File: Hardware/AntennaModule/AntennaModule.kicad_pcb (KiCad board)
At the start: 2 copper layers, 53 parts, among them J1 Conn_01x10, SW1 ColdStart, U1 C0727J5003AHF-1, U2 C0727J5003AHF-1, U3 NJG1155UX2, U4 NT1192FAAE1S, U5 PD0922J5050S2HF, U6 NT1192FAAE1S, U7 NEO-D9C, U8 NEO-F9P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

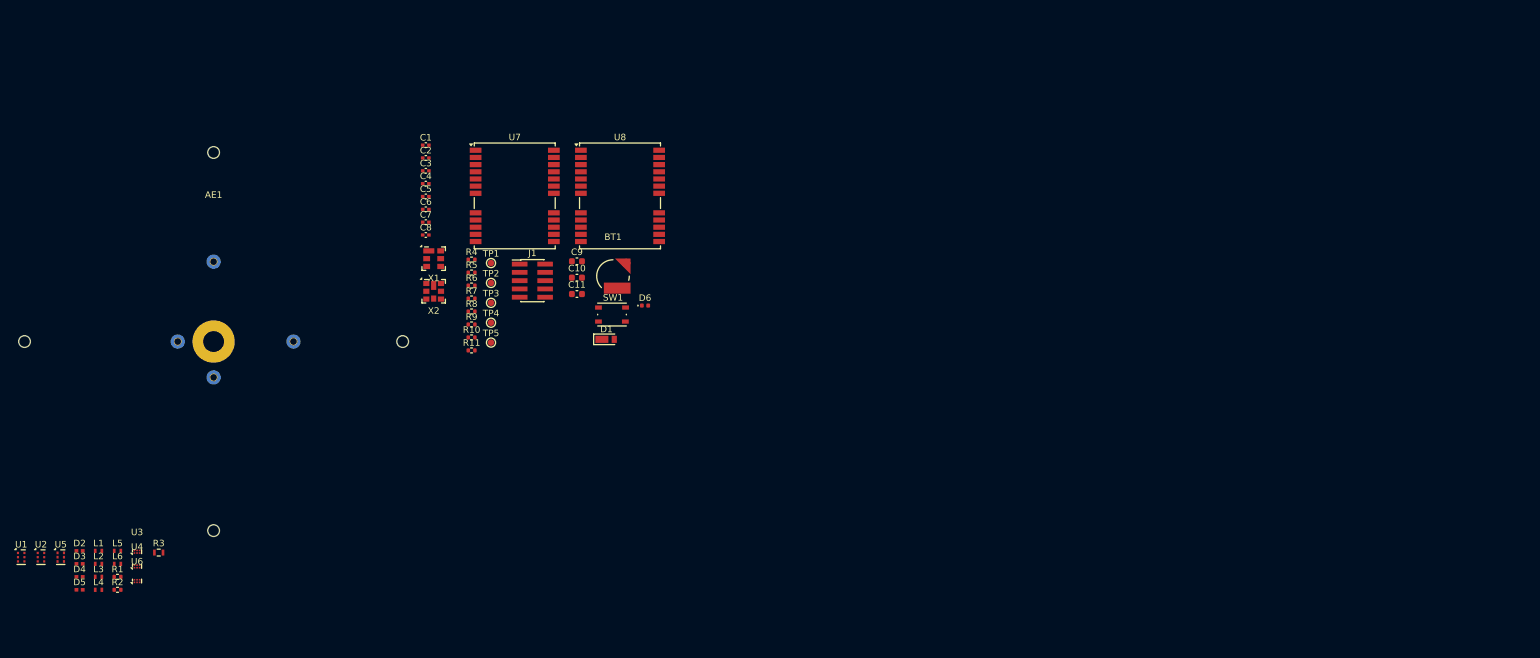
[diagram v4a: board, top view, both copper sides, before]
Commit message: グリッドとドリルの原点を設定
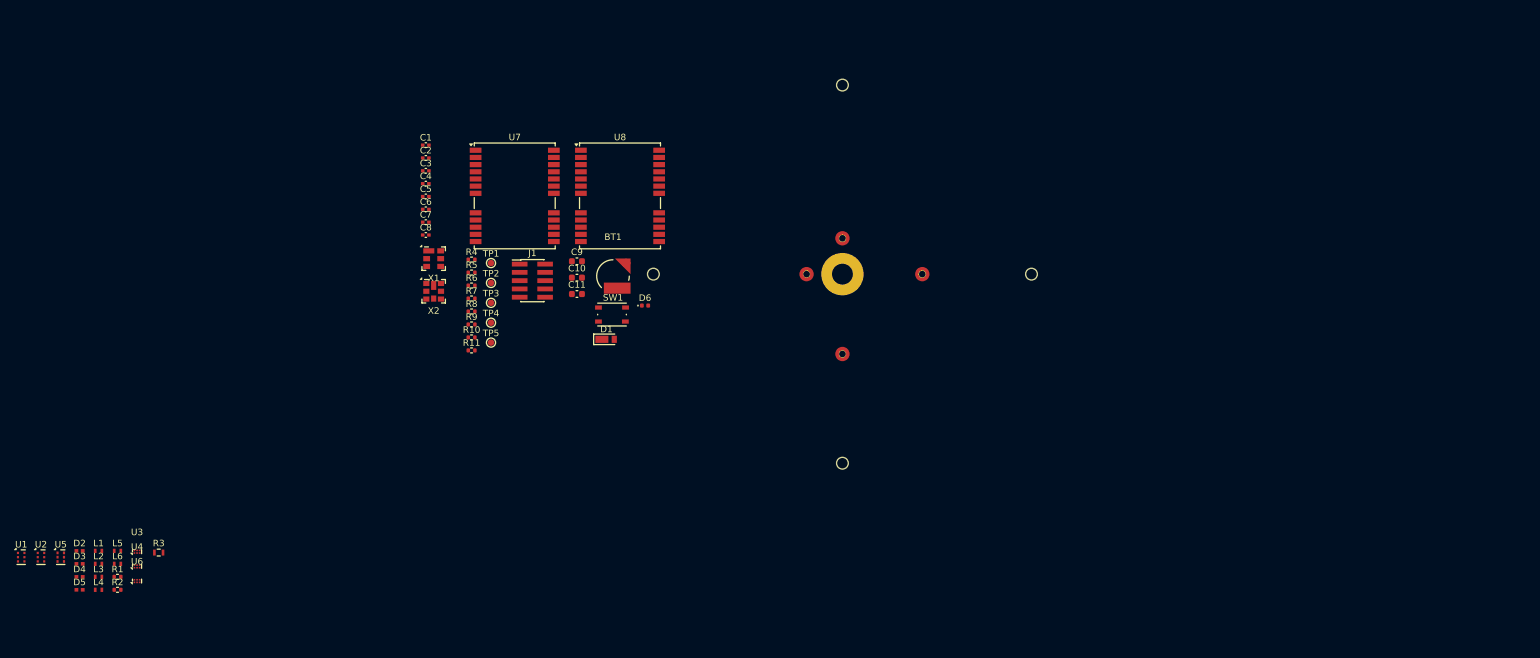
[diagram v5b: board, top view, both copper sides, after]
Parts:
- AE1: moved to B.Cu
- moved AE1 97.0 mm to (150.0, 100.0)

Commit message: 部品配置決定
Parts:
- moved U5 138.3 mm to (164.0, 108.9), turned to 90 degrees
- moved L1 137.8 mm to (162.7, 88.6), turned to -90 degrees
- moved L3 136.9 mm to (162.7, 94.9), turned to -90 degrees
- moved U1 136.4 mm to (150.0, 91.1), turned to -90 degrees
- moved L4 135.7 mm to (162.7, 100.0), turned to 90 degrees
- moved L5 135.4 mm to (166.5, 97.5)
- moved L6 133.8 mm to (167.8, 108.9), turned to -90 degrees
- moved D3 133.4 mm to (156.3, 93.7), turned to 180 degrees
- moved L2 131.6 mm to (164.0, 114.0), turned to 90 degrees
- moved U3 131.4 mm to (162.7, 91.1)
- moved U6 130.9 mm to (167.8, 111.4)
- moved D4 128.6 mm to (156.3, 110.2), turned to -90 degrees
- moved U2 127.0 mm to (150.0, 111.4), turned to 90 degrees
- moved U4 126.7 mm to (164.0, 111.4), turned to 180 degrees
- moved R3 124.3 mm to (164.0, 106.3)
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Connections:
- C8 pad 1: Net-(U5-Output1) -> Net-(U5-Output2)
- L4 pad 1: Net-(U5-Output1) -> Net-(U5-Output2)
- R3 pad 1: Net-(U5-Output1) -> Net-(U5-Output2)
- R3 pad 2: Net-(U5-Output2) -> Net-(U5-Output1)
- X1 pad 2: Net-(U5-Output2) -> Net-(U5-Output1)
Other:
- board outline added: 80 x 80 mm

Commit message: スタックアップを決定
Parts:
- moved D2 4.93 mm to (148.6, 93.7), turned to 0 degrees
- moved D3 4.29 mm to (152.1, 93.7), turned to 0 degrees
- moved TP2 4.02 mm to (172.9, 100.0)
- moved C9 4.02 mm to (188.1, 92.4)
- moved R6 4.02 mm to (188.1, 94.9)
- moved R9 4.02 mm to (188.1, 96.2)
- moved U5 3.86 mm to (164.6, 105.1)
- moved L2 3.24 mm to (164.6, 110.8)
- moved R3 3.24 mm to (164.6, 103.2)
- moved C6 2.84 mm to (167.8, 108.9)
- moved U6 2.84 mm to (169.1, 108.9)
- moved R10 2.84 mm to (188.1, 106.3)
- moved R7 2.84 mm to (188.1, 105.1)
- moved TP4 2.84 mm to (188.1, 108.9)
- moved C4 2.62 mm to (165.9, 108.9)
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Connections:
- C3 pad 1: +3.3VA -> +3.3VP
- U3 pad 2: +3.3VA -> +3.3VP
- U3 pad 6: +3.3VA -> +3.3VP
- U7 pad 9: unconnected-(U7-VCC_RF-Pad9) -> +3.3VA
- U8 pad 9: +3.3VA -> +3.3VP
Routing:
- net /RF_IN_D9C: track 0.00 -> 8.05 mm
- net Net-(U2-Input): track 0.00 -> 2.03 mm
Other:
- copper layers 2 -> 4
- board text added: "0"
- board text added: "0 mm"
- board text added: "0.01 mm"
- board text added: "0.0152 mm"
- board text added: "0.02"
- board text added: "0.035 mm"
- board text added: "0.1000 mm / 0.1000 mm"
- board text added: "0.1164 mm"
- board text added: "0.1500 mm"
- board text added: "0.218 mm"
- board text added: "0.4 mm"
- board text added: "0.4mm H/HOZ without copper"
- board text added: "1"
- board text added: "1.6252 mm"
- board text added: "2116 RC54% 4.9mil"
- board text added: "3.8"
- board text added: "4"
- board text added: "4.4"
- board text added: "4.6"
- board text added: "7628, RC 49%, 8.6 mil"
- board text added: "80.0025 mm x 80.0025 mm"
- board text added: "B.Cu"
- board text added: "B.Mask"
- board text added: "B.Paste"
- board text added: "B.Silkscreen"
- board text added: "Bottom Silk Screen"
- board text added: "Bottom Solder Mask"
- board text added: "Bottom Solder Paste"
- board text added: "ENIG"
- board text added: "F.Cu"
- board text added: "F.Mask"
- board text added: "F.Paste"
- board text added: "F.Silkscreen"
- board text added: "In1.Cu"
- board text added: "In2.Cu"
- board text added: "JLC04161H-7628B"
- board text added: "Not specified"
- board text added: "RFINパッドの高さを揃える"
- board text added: "Top Silk Screen"
- board text added: "Top Solder Mask"
- board text added: "Top Solder Paste"
- board text added: "copper"
- board text added: "core"
- board text added: "prepreg"
- board text added: "εR"
- board text added: "いいえ"
- board text added: "はい"
- board text added: "インピーダンス制御:"
- board text added: "エッジ カード コネクタ:"
- board text added: "カラー"
- board text added: "タイプ"
- board text added: "レイヤー名"
- board text added: "基板の特性"
- board text added: "基板全体の寸法:"
- board text added: "基板厚:"
- board text added: "基板端メッキ:"
- board text added: "導体レイヤー数:"
- board text added: "損失正接"
- board text added: "曲げ半径は配線幅の3倍以上 抵抗の中心xは接続するパッドの中心xから外側に0.145オフセット 下側TVSダイオード位置合わせ済"
- board text added: "最小穴径:"
- board text added: "最小配線幅/間隔:"
- board text added: "材料"
- board text added: "端面スルーホール パッド:"
- board text added: "線幅 (mm)"
- board text added: "誘電体 1 (1/3)"
- board text added: "誘電体 2"
- board text added: "誘電体 3 (1/3)"
- board text added: "銅箔仕上げ:"

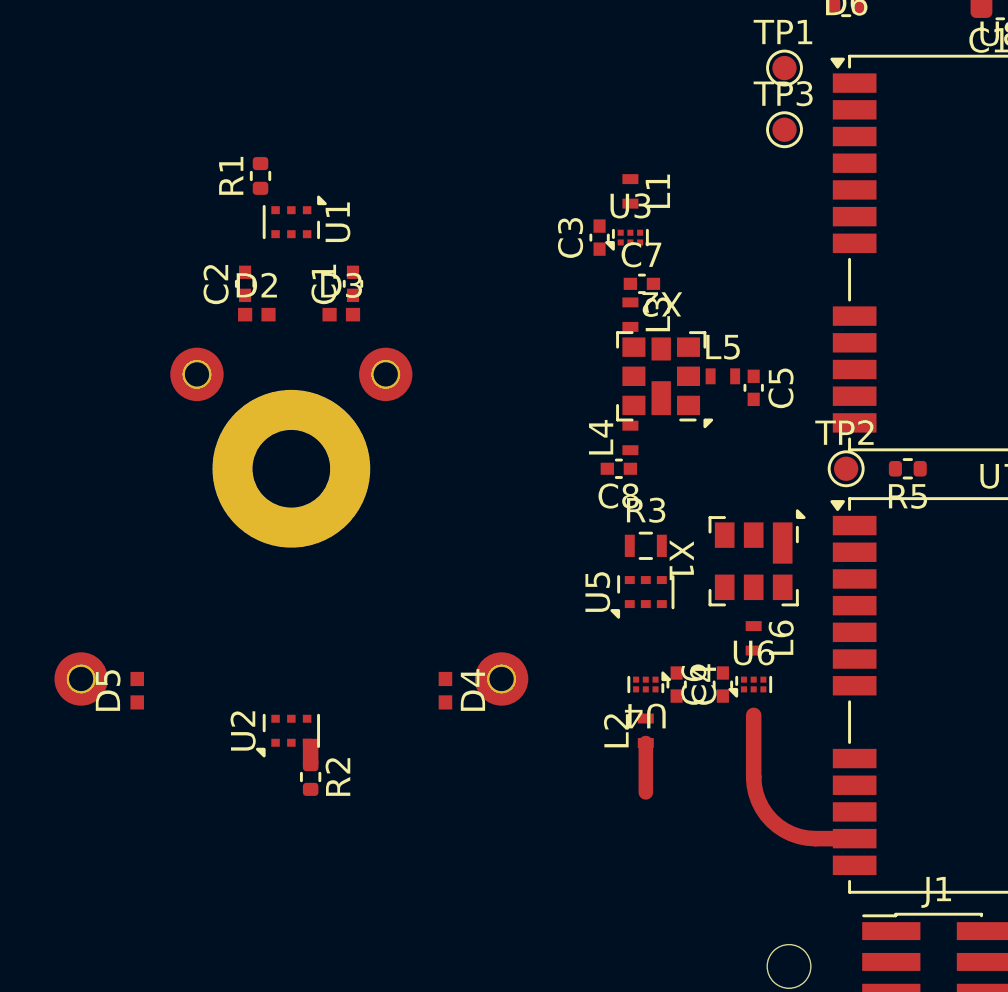
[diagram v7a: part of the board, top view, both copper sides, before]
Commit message: 円弧配線に対応
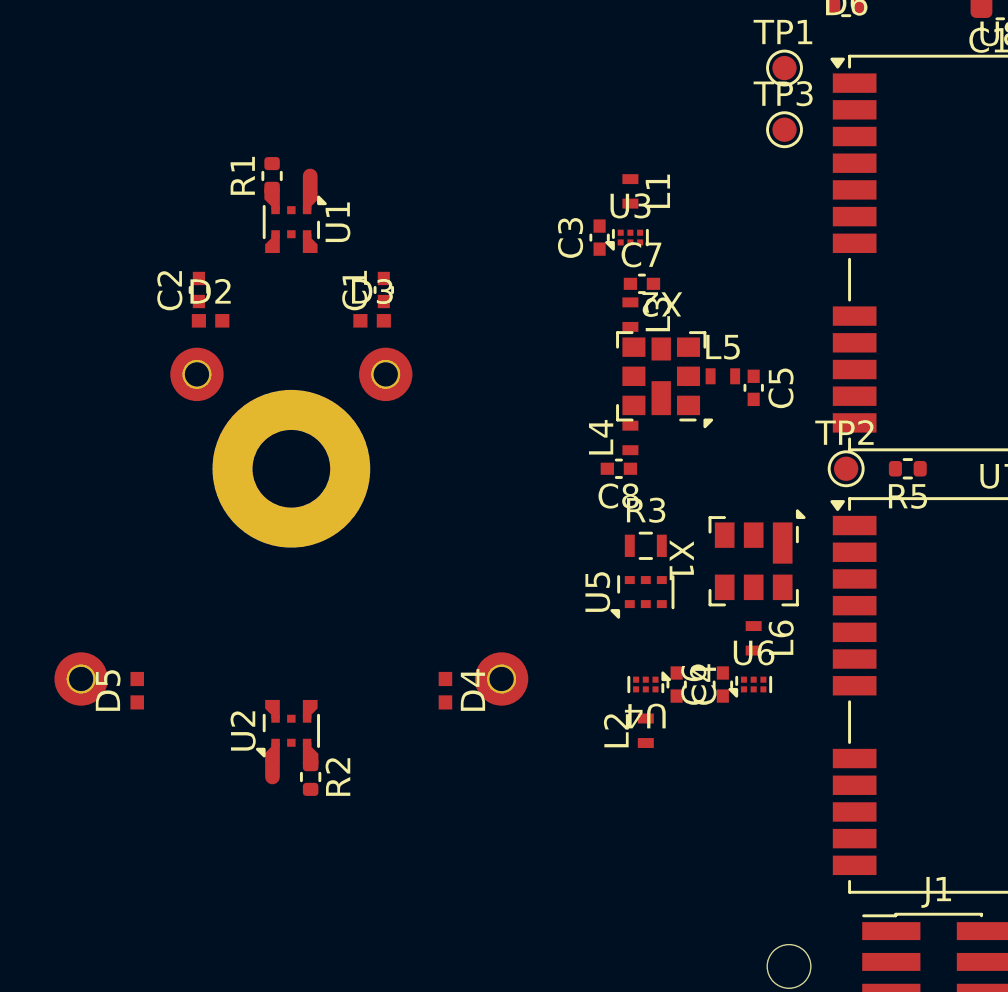
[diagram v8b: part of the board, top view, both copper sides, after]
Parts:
- moved C2 1.92 mm to (146.2, 92.6)
- moved D2 1.92 mm to (146.7, 93.9)
- moved C1 1.30 mm to (153.8, 92.6)
- moved D3 1.30 mm to (153.3, 93.9)
- moved R1 0.48 mm to (149.2, 87.9)
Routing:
- net /RF_IN_D9C: track 8.05 -> 0.00 mm
- net Net-(U2-Input): track 2.03 -> 0.64 mm
- net Net-(U1-Input): track 0.00 -> 0.63 mm
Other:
- board text added: "-(0.605-0.35)/2 カプラのパッドX位置から伝送線路X位置のオフセット"
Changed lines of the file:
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@@
 	(footprint "Resistor_SMD:R_0402_1005Metric"
 		(layer "F.Cu")
-		(at 148.73 87.935 90)
+		(at 149.205 87.935 90)
 		(descr "Resistor SMD 0402 (1005 Metric), square (rectangular) end terminal, IPC_7351 nominal, (Body size source: IPC-SM-782 page 72, https://www.pcb-3d.com/wordpress/wp-content/uploads/ipc-sm-782a_amendment_1_and_2.pdf), generated with kicad-footprint-generator")
 		(tags "resistor")
@@
 	(footprint "Diode_SMD_extlib:D_Littelfuse_AXGD10402KR_0402_1005Metric_1.02x0.51mm"
 		(layer "F.Cu")
-		(at 148.5776 93.65)
+		(at 146.6726 93.904)
 		(descr "TVS Diode, Littelfuse, AXGD series, 0402 (1005 Metric) (https://www.littelfuse.co.jp/products/polymer-esd-suppressors/xtremeguard-esd-suppressors/axgd/axgd10402kr.aspx)")
 		(tags "chip TVS ESD Diode Littelfuse AXGD")
@@
 	(footprint "Capacitor_SMD_extlib:C_Murata_xxx15_0402_1005Metric_1.0x0.5mm"
 		(layer "F.Cu")
-		(at 152.54 92.38 90)
+		(at 153.81 92.634 90)
 		(descr "Capacitor, Murata, 0402 (1005 Metric) (https://search.murata.co.jp/Ceramy/image/img/A01X/G101/JPN/GJM1555C1H4R7WB01-01A.pdf)")
 		(tags "chip capacitor Murata GRM15 GJM15 GQM15")
@@
 	(footprint "Capacitor_SMD_extlib:C_Murata_xxx15_0402_1005Metric_1.0x0.5mm"
 		(layer "F.Cu")
-		(at 148.095 92.38 90)
+		(at 146.19 92.634 90)
 		(descr "Capacitor, Murata, 0402 (1005 Metric) (https://search.murata.co.jp/Ceramy/image/img/A01X/G101/JPN/GJM1555C1H4R7WB01-01A.pdf)")
 		(tags "chip capacitor Murata GRM15 GJM15 GQM15")
@@
 	(footprint "Diode_SMD_extlib:D_Littelfuse_AXGD10402KR_0402_1005Metric_1.02x0.51mm"
 		(layer "F.Cu")
-		(at 152.0574 93.65)
+		(at 153.3274 93.904)
 		(descr "TVS Diode, Littelfuse, AXGD series, 0402 (1005 Metric) (https://www.littelfuse.co.jp/products/polymer-esd-suppressors/xtremeguard-esd-suppressors/axgd/axgd10402kr.aspx)")
 		(tags "chip TVS ESD Diode Littelfuse AXGD")
@@
 	(gr_poly
 		(pts
-			(xy 150.475 112.190001) (xy 151.115 112.190001) (xy 151.115 111.1252) (xy 150.475 111.1252)
+			(xy 150.475001 110.300001) (xy 150.825 110.300001) (xy 150.825 110.135) (xy 151.08 109.88) (xy 151.08 109.525)
+			(xy 150.475 109.524999)
+		)
+		(stroke
+			(width 0)
+			(type default)
+		)
+		(fill solid)
+		(layer "F.Cu")
+		(net 2)
+	)
+	(gr_poly
+		(pts
+			(xy 150.475001 90.334999) (xy 150.825 90.334999) (xy 150.825 90.5) (xy 151.08 90.755) (xy 151.08 91.11)
+			(xy 150.475 91.110001)
+		)
+		(stroke
+			(width 0)
+			(type default)
+		)
+		(fill solid)
+		(layer "F.Cu")
+		(net 8)
+	)
+	(gr_poly
+		(pts
+			(xy 149.524999 110.300001) (xy 149.175 110.300001) (xy 149.175 110.135) (xy 148.92 109.88) (xy 148.92 109.525)
+			(xy 149.525 109.524999)
+		)
+		(stroke
+			(width 0)
+			(type default)
+		)
+		(fill solid)
+		(layer "F.Cu")
+		(net 4)
+	)
+	(gr_poly
+		(pts
+			(xy 150.475 112.190001) (xy 151.115 112.190001) (xy 151.115 111.745) (xy 150.825 111.455) (xy 150.825 111.289999)
+			(xy 150.475 111.289999)
 		)
 		(stroke
@@
 		(net 35)
 	)
+	(gr_poly
+		(pts
+			(xy 150.475001 89.345001) (xy 150.825 89.345001) (xy 150.825 89.18) (xy 151.08 88.925) (xy 151.08 88.57)
+			(xy 150.475 88.569999)
+		)
+		(stroke
+			(width 0)
+			(type default)
+		)
+		(fill solid)
+		(layer "F.Cu")
+		(net 25)
+	)
+	(gr_poly
+		(pts
+			(xy 149.524999 90.334999) (xy 149.175 90.334999) (xy 149.175 90.5) (xy 148.92 90.755) (xy 148.92 91.11)
+			(xy 149.525 91.110001)
+		)
+		(stroke
+			(width 0)
+			(type default)
+		)
+		(fill solid)
+		(layer "F.Cu")
+		(net 9)
+	)
+	(gr_poly
+		(pts
+			(xy 149.524999 111.289999) (xy 149.175 111.289999) (xy 149.175 111.455) (xy 148.92 111.71) (xy 148.92 112.065)
+			(xy 149.525 112.065001)
+		)
+		(stroke
+			(width 0)
+			(type default)
+		)
+		(fill solid)
+		(layer "F.Cu")
+		(net 28)
+	)
+	(gr_poly
+		(pts
+			(xy 149.525 88.444999) (xy 148.885 88.444999) (xy 148.885 88.89) (xy 149.175 89.18) (xy 149.175 89.345001)
+			(xy 149.525 89.345001)
+		)
+		(stroke
+			(width 0)
+			(type default)
+		)
+		(fill solid)
+		(layer "F.Cu")
+		(net 34)
+	)
 	(gr_line
 		(start 148.73 115.24)
@@
 	)
 	(gr_line
+		(start 151.016 110.16)
+		(end 155.08 110.16)
+		(stroke
+			(width 0.1)
+			(type default)
+		)
+		(layer "Cmts.User")
+	)
+	(gr_line
 		(start 210 101.52)
 		(end 337.385714 101.52)
@@
 		)
 	)
+	(gr_text "-(0.605-0.35)/2\nカプラのパッドX位置から伝送線路X位置のオフセット"
+		(at 132.1175 126.67 0)
+		(layer "Cmts.User")
+		(effects
+			(font
+				(size 1 1)
+				(thickness 0.15)
+			)
+			(justify left bottom)
+		)
+	)
 	(gr_text "0.035 mm"
 		(at 291.107143 105.876 0)
@@
 	)
 	(segment
-		(start 164.605 111.3)
-		(end 164.605 113.335)
-		(width 0.6)
+		(start 150.7775 87.935)
+		(end 150.7775 88.57)
+		(width 0.605)
 		(layer "F.Cu")
-		(net 28)
+		(net 25)
 	)
 	(segment
-		(start 169.05 112.7)
-		(end 169.05 110.16)
-		(width 0.64)
+		(start 149.2225 112.065)
+		(end 149.2225 112.7)
+		(width 0.605)
 		(layer "F.Cu")
-		(net 52)
-	)
-	(segment
-		(start 173.21 115.24)
-		(end 171.59 115.24)
-		(width 0.64)
-		(layer "F.Cu")
-		(net 52)
-	)
-	(arc
-		(start 171.59 115.24)
-		(mid 169.793949 114.496051)
-		(end 169.05 112.7)
-		(width 0.64)
-		(layer "F.Cu")
-		(net 52)
+		(net 28)
 	)
 	(group "group-boardCharacteristics"
